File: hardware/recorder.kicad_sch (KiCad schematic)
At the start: 19 parts, among them J1 Nano TX V2, J2 Buck MP1584E, J3 LiPo 3S / PSU, J4 USB-Serial, SW1 SW_Push, SW2 SW_Push, SW3 SW_SPST, U1 Raspberry Pi Pico

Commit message: Add the fuse and decoupling capacitors the schematic was missing
The circuit had no passives on the power rails at all. They are cheap
insurance and awkward to retrofit once a board exists, so add them
before layout:

- F1 in series on LiPo+ ahead of everything (2A as a starting value;
  the real rating needs measuring)
- C1 470uF/25V + C2 100nF on the VBAT rail, for the voltage dip when
  the TX module transmits. 25V so a full 3S pack has margin.
- C3 100uF/16V + C4 100nF on the 5V rail, for gamepad inrush

Verified the same way as before: ERC clean, and the netlist confirms
F1 is genuinely in series (J3.1 -> F1 -> VBAT_7_13V) rather than
bridged across it, with every capacitor between its rail and ground.

Also hides the #PWR references, which KiCad normally does and which
were cluttering the drawing.

Co-Authored-By: Claude Opus 5 <noreply@anthropic.com>
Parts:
- added C1: 470uF/25V, symbol Device:C_Polarized
- added C2, C4: 100nF, symbol Device:C
- added C3: 100uF/16V, symbol Device:C_Polarized
- added F1: 2A, symbol Device:Fuse
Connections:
- net +5V: now also C3.1, C4.1
- net GND: now also C1.2, C2.2, C3.2, C4.2
- net VBAT_7_13V: now also C1.1, C2.1, F1.1; no longer J3.1 (Pin_1)
- new net: F1.2, J3.1 (Pin_1)
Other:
- note added: "C1/C2: Nano TX VBAT直近に置く（送信バーストの電圧ドロップ対策）"
- note added: "C3/C4: Pico VBUS直近に置く（ゲームパッド接続時の突入電流対策）"
- note added: "⚠️ 電解コンの耐圧は3S満充電12.6Vを超えること。極性に注意"

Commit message: Add 5V TVS and a series resistor on GP1, plus a design review pass
Requested TVS (D6) across the 5V rail: if the buck fails short, 12V
reaches the rail at a current the fuse considers normal, so nothing
disconnects it. D6 conducts and pulls enough current to blow F1. Uses
a bidirectional part to match KiCad's bidirectional TVS symbol, which
also removes a polarity to get wrong at assembly. Documented honestly:
its ~9V clamp is above the Pico's 5.5V maximum, so this ends the fault
rather than saving the Pico.

Review of the rest turned up one more thing worth a part: GP1 ran
straight to the CRSF bus with no resistor, so plugging J1 in backwards
would put up to 13V directly on a GPIO (GP0 at least had the 680R).
Added R7 1k, which at 921600bps costs a few ns of edge.

Remaining findings are ones parts cannot fix -- reverse polarity on
the LiPo connector, J1 keying, the provisional 2A fuse rating, LED
current slightly over the GPIO drive setting -- and are written up in
hardware/README.md along with the layout points they imply.

Co-Authored-By: Claude Opus 5 <noreply@anthropic.com>
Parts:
- added D6: SMAJ5.0CA, symbol Device:D_TVS
- added R7: 1k, symbol Device:R
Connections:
- net +5V: now also D6.2 (A2)
- net CRSF_BUS: now also R7.1; no longer U1.2 (GPIO1)
- net GND: now also D6.1 (A1)
- new net: R7.2, U1.2 (GPIO1)
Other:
- note added: "D6: Buck短絡故障時に12Vが5Vへ出るのを断つ（ヒューズを飛ばす）"

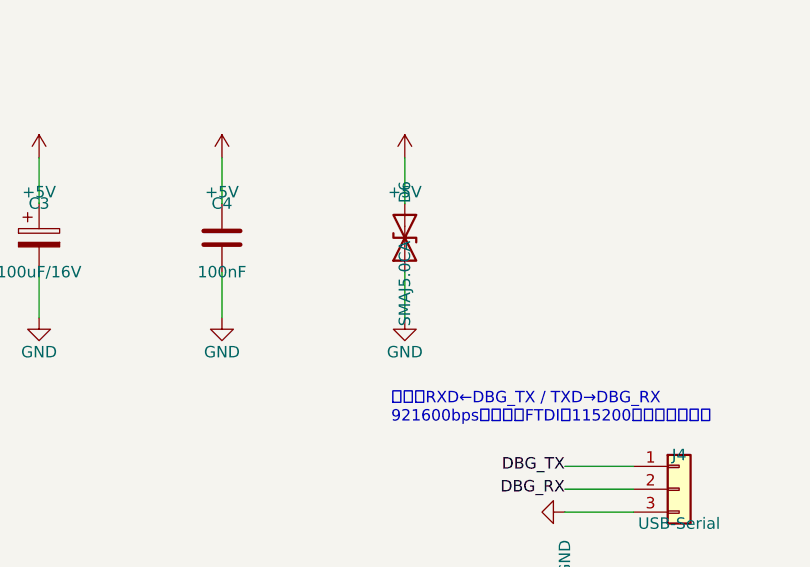
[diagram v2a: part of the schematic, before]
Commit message: Design the PCB: 105x85mm two-layer board, DRC clean
Lays out and routes the board from the existing schematic. Generated
by script the same way the schematic was, and checked mechanically
rather than by eye: DRC reports 0 violations and 0 unconnected items,
and Gerber export succeeds.

Layout choices that made the routing tractable:
- Everything is through-hole, so the bottom-side ground pour reaches
  every GND pad directly -- no ground tracks and no vias anywhere.
- Parts that land on the Pico's left pin row sit to its left and the
  buck (VBUS) to its right, so nothing has to cross the module.
- Left-hand parts are placed at the same Y as the pin they serve, so
  those nets are straight horizontal runs that cannot cross.
- VBAT is kept short and +5V takes the long way to the Pico, since
  VBAT carries the larger current (the 65mm 5V run drops ~20mV).

The generator self-checks that every track endpoint lands on a pad of
its net or joins another track of the same net, which caught several
coordinate errors. Two KiCad behaviours worth recording: same-numbered
pads (fuse holder, tact switches) are not treated as internally
connected and need copper between them, and kicad-cli cannot fill
zones, so fill_zones.py drives pcbnew to do it before DRC.

Adds a custom Pico footprint (2x20 headers, 17.78mm rows) since KiCad
ships none, plus fp-lib-table so the project finds it.

Not ordered and not verified in copper. J2's footprint is a
placeholder until the buck module is measured; hardware/README.md
lists that and the rest of the pre-order checks.

Co-Authored-By: Claude Opus 5 <noreply@anthropic.com>
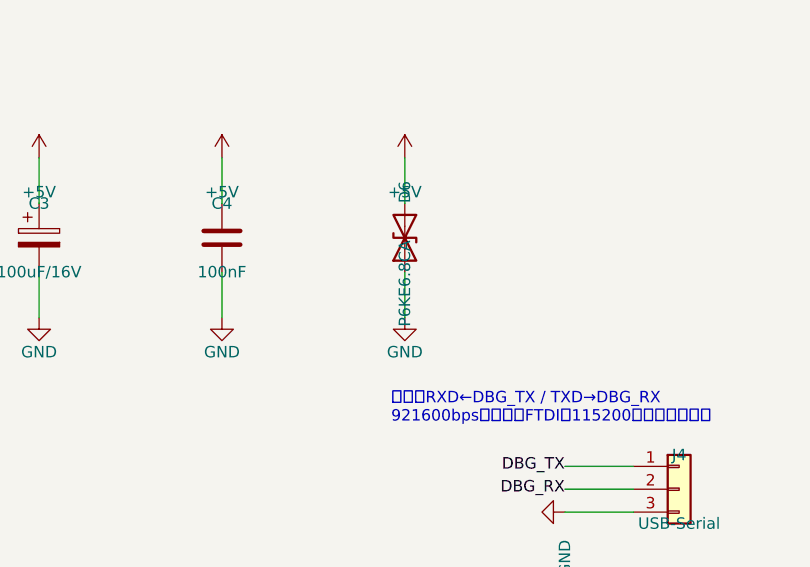
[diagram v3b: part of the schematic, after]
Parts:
- C1: footprint (none) -> Capacitor_THT:CP_Radial_D10.0mm_P5.00mm
- C2, C4: footprint (none) -> Capacitor_THT:C_Disc_D5.0mm_W2.5mm_P5.00mm
- C3: footprint (none) -> Capacitor_THT:CP_Radial_D6.3mm_P2.50mm
- D1, D2, D3, D4, D5: footprint (none) -> LED_THT:LED_D3.0mm
- D6: value SMAJ5.0CA -> P6KE6.8CA; footprint (none) -> Diode_THT:D_DO-15_P10.16mm_Horizontal
- F1: footprint (none) -> Fuse:Fuseholder_Blade_Mini_Keystone_3568
- J1: footprint (none) -> Connector_JST:JST_XH_B3B-XH-A_1x03_P2.50mm_Vertical
- J2: footprint (none) -> Connector_PinHeader_2.54mm:PinHeader_1x04_P2.54mm_Vertical
- J3: footprint (none) -> Connector_Wire:SolderWire-0.75sqmm_1x02_P7mm_D1.25mm_OD3.5mm
- J4: footprint (none) -> Connector_PinHeader_2.54mm:PinHeader_1x03_P2.54mm_Vertical
- R1, R2, R3, R4, R5, R6, R7: footprint (none) -> Resistor_THT:R_Axial_DIN0207_L6.3mm_D2.5mm_P10.16mm_Horizontal
- SW1, SW2: footprint (none) -> Button_Switch_THT:SW_PUSH_6mm
- SW3: footprint (none) -> Button_Switch_THT:SW_DIP_SPSTx01_Slide_9.78x4.72mm_W7.62mm_P2.54mm
- U1: footprint (none) -> recorder:RPi_Pico_Headers
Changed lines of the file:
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@@
       )
     )
-    (property "Footprint" ""
+    (property "Footprint" "recorder:RPi_Pico_Headers"
       (at 139.7 109.22 0)
       (effects
@@
       )
     )
-    (property "Footprint" ""
+    (property "Footprint" "Resistor_THT:R_Axial_DIN0207_L6.3mm_D2.5mm_P10.16mm_Horizontal"
       (at 104.14 96.52 0)
       (effects
@@
       )
     )
-    (property "Footprint" ""
+    (property "Footprint" "Resistor_THT:R_Axial_DIN0207_L6.3mm_D2.5mm_P10.16mm_Horizontal"
       (at 243.84 60.96 0)
       (effects
@@
       )
     )
-    (property "Footprint" ""
+    (property "Footprint" "LED_THT:LED_D3.0mm"
       (at 259.08 60.96 0)
       (effects
@@
       )
     )
-    (property "Footprint" ""
+    (property "Footprint" "Resistor_THT:R_Axial_DIN0207_L6.3mm_D2.5mm_P10.16mm_Horizontal"
       (at 243.84 76.2 0)
       (effects
@@
       )
     )
-    (property "Footprint" ""
+    (property "Footprint" "LED_THT:LED_D3.0mm"
       (at 259.08 76.2 0)
       (effects
@@
       )
     )
-    (property "Footprint" ""
+    (property "Footprint" "Resistor_THT:R_Axial_DIN0207_L6.3mm_D2.5mm_P10.16mm_Horizontal"
       (at 243.84 91.44 0)
       (effects
@@
       )
     )
-    (property "Footprint" ""
+    (property "Footprint" "LED_THT:LED_D3.0mm"
       (at 259.08 91.44 0)
       (effects
@@
       )
     )
-    (property "Footprint" ""
+    (property "Footprint" "Resistor_THT:R_Axial_DIN0207_L6.3mm_D2.5mm_P10.16mm_Horizontal"
       (at 243.84 106.68 0)
       (effects
@@
       )
     )
-    (property "Footprint" ""
+    (property "Footprint" "LED_THT:LED_D3.0mm"
       (at 259.08 106.68 0)
       (effects
@@
       )
     )
-    (property "Footprint" ""
+    (property "Footprint" "Resistor_THT:R_Axial_DIN0207_L6.3mm_D2.5mm_P10.16mm_Horizontal"
       (at 243.84 121.92 0)
       (effects
@@
       )
     )
-    (property "Footprint" ""
+    (property "Footprint" "LED_THT:LED_D3.0mm"
       (at 259.08 121.92 0)
       (effects
@@
       )
     )
-    (property "Footprint" ""
+    (property "Footprint" "Button_Switch_THT:SW_PUSH_6mm"
       (at 55.88 71.12 0)
       (effects
@@
       )
     )
-    (property "Footprint" ""
+    (property "Footprint" "Button_Switch_THT:SW_PUSH_6mm"
       (at 55.88 91.44 0)
       (effects
@@
       )
     )
-    (property "Footprint" ""
+    (property "Footprint" "Button_Switch_THT:SW_DIP_SPSTx01_Slide_9.78x4.72mm_W7.62mm_P2.54mm"
       (at 55.88 111.76 0)
       (effects
@@
       )
     )
-    (property "Footprint" ""
+    (property "Footprint" "Connector_JST:JST_XH_B3B-XH-A_1x03_P2.50mm_Vertical"
       (at 243.84 144.78 0)
       (effects
@@
       )
     )
-    (property "Footprint" ""
+    (property "Footprint" "Resistor_THT:R_Axial_DIN0207_L6.3mm_D2.5mm_P10.16mm_Horizontal"
       (at 218.44 142.24 0)
       (effects
@@
       )
     )
-    (property "Footprint" ""
+    (property "Footprint" "Connector_PinHeader_2.54mm:PinHeader_1x04_P2.54mm_Vertical"
       (at 60.96 160.02 0)
       (effects
@@
       )
     )
-    (property "Footprint" ""
+    (property "Footprint" "Connector_Wire:SolderWire-0.75sqmm_1x02_P7mm_D1.25mm_OD3.5mm"
       (at 60.96 205.74 0)
       (effects
@@
       )
     )
-    (property "Footprint" ""
+    (property "Footprint" "Fuse:Fuseholder_Blade_Mini_Keystone_3568"
       (at 40.64 205.74 0)
       (effects
@@
       )
     )
-    (property "Footprint" ""
+    (property "Footprint" "Capacitor_THT:CP_Radial_D10.0mm_P5.00mm"
       (at 132.08 187.96 0)
       (effects
@@
       )
     )
-    (property "Footprint" ""
+    (property "Footprint" "Capacitor_THT:C_Disc_D5.0mm_W2.5mm_P5.00mm"
       (at 152.4 187.96 0)
       (effects
@@
       )
     )
-    (property "Footprint" ""
+    (property "Footprint" "Capacitor_THT:CP_Radial_D6.3mm_P2.50mm"
       (at 172.72000000000003 187.96 0)
       (effects
@@
       )
     )
-    (property "Footprint" ""
+    (property "Footprint" "Capacitor_THT:C_Disc_D5.0mm_W2.5mm_P5.00mm"
       (at 193.04000000000002 187.96 0)
       (effects
@@
       )
     )
-    (property "Value" "SMAJ5.0CA"
+    (property "Value" "P6KE6.8CA"
       (at 213.36 193.04 0)
       (effects
@@
       )
     )
-    (property "Footprint" ""
+    (property "Footprint" "Diode_THT:D_DO-15_P10.16mm_Horizontal"
       (at 213.36 187.96 0)
       (effects
@@
       )
     )
-    (property "Footprint" ""
+    (property "Footprint" "Connector_PinHeader_2.54mm:PinHeader_1x03_P2.54mm_Vertical"
       (at 243.84 215.9 0)
       (effects

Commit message: Fit the real MP1584EN buck module: custom footprint and re-layout
The module arrived, so J2 is no longer a placeholder header. Derived
its footprint from the product photos by measuring the pad positions
in the image rather than eyeballing them: eight holes in four pairs,
board 22.3x16.8mm, columns at +/-9.45mm and rows at +/-6.70/4.16mm
with the expected 2.54mm pair pitch, symmetric about the centre.

Pin orientation comes from both photos agreeing: the underside silk
reads OUT-/IN- over OUT+/IN+, which mirrors to IN on the left and OUT
on the right seen from the component side, matching the board's own
+/- marks sitting on the output end.

Moving to a 22.3mm-wide part meant re-placing J2 (it would have sat on
top of the Pico at the old position) and rerouting VBAT and +5V. The
module now sits bottom-right, clear of both the Pico and the corner
mounting hole, whose courtyard is a 3.45mm circle and caught the first
two attempts.

Still DRC clean: 0 violations, 0 unconnected, ERC 0/0, Gerbers export.

The dimensions come from image analysis, not calipers, so README now
says to check the eight holes against a 1:1 printout before ordering
and which two constants to edit if they are off.

Co-Authored-By: Claude Opus 5 <noreply@anthropic.com>
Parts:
- J2: footprint Connector_PinHeader_2.54mm:PinHeader_1x04_P2.54mm_Vertical -> recorder:MP1584EN_Module
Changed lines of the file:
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@@
       )
     )
-    (property "Footprint" "Connector_PinHeader_2.54mm:PinHeader_1x04_P2.54mm_Vertical"
+    (property "Footprint" "recorder:MP1584EN_Module"
       (at 60.96 160.02 0)
       (effects
